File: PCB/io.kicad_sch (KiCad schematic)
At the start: 18 parts, among them J1 Conn_ARM_SWD_TagConnect_TC203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, J2 USB_C_Receptacle_USB2.0_16P, Q4 PMOS, U5 TLC59283RGER

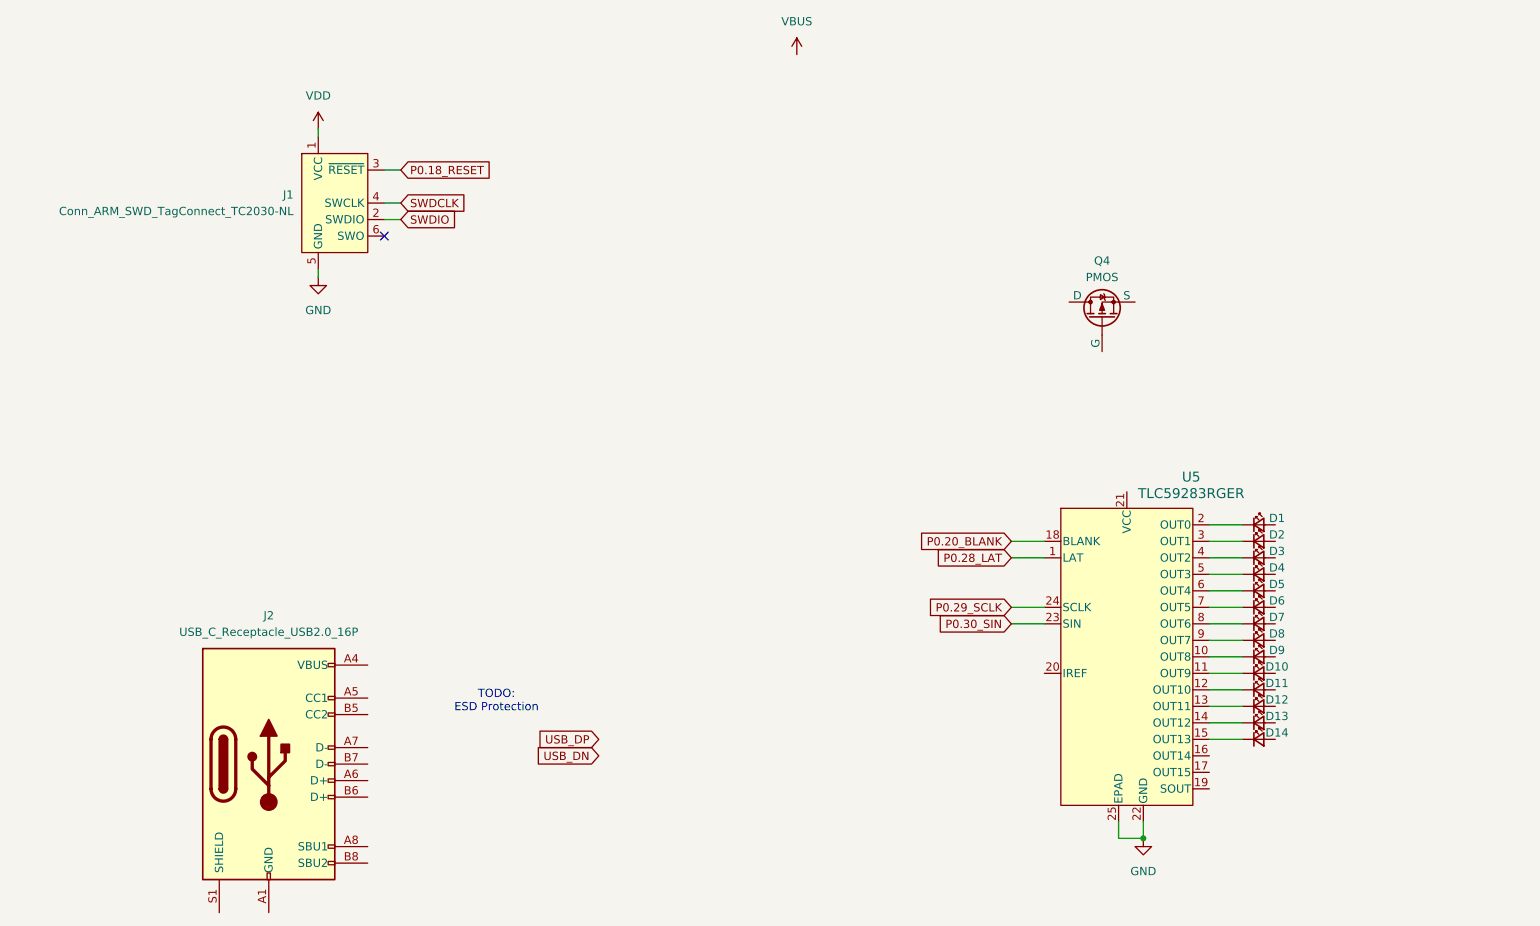
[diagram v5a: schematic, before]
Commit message: redid the pcb layout for a more bigger devboard approach. Added a few more components and the antenna.
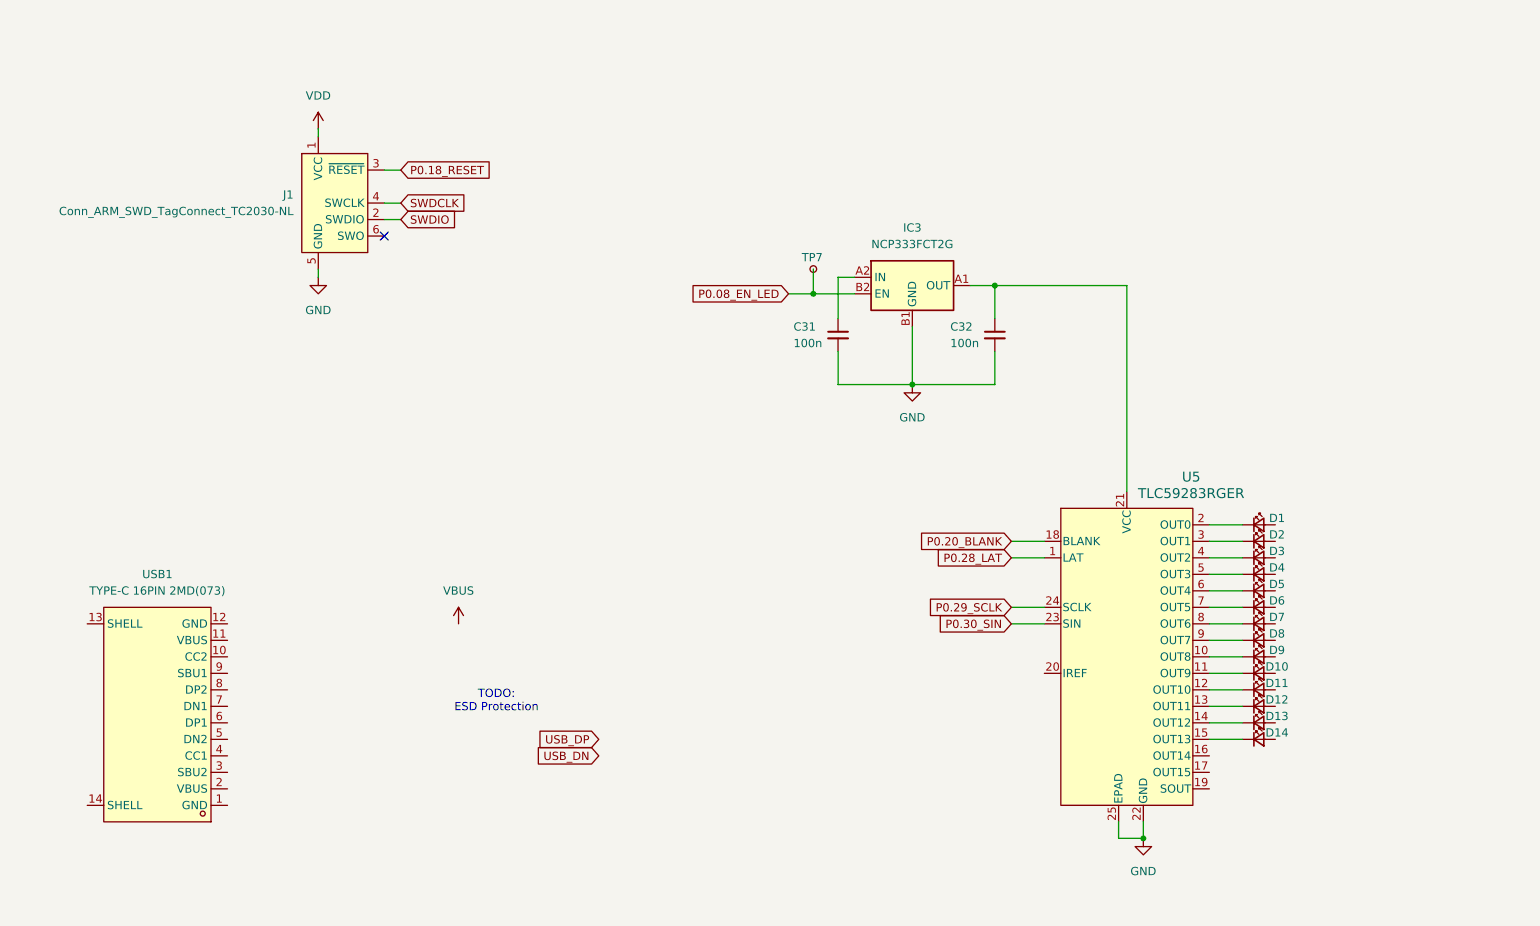
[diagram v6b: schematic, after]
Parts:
- removed J2: USB_C_Receptacle_USB2.0_16P, symbol Connector:USB_C_Receptacle_USB2.0_16P
- removed Q4: PMOS, symbol Simulation_SPICE:PMOS
- added C31, C32: 100n, Capacitor_SMD:C_0402_1005Metric, symbol Device:C_Small
- added IC3: NCP333FCT2G, BGA4C40P2X2_76X76X63, symbol NCP333FCT2G:NCP333FCT2G
- added TP7: TestPoint_Small, TestPoint:TestPoint_Pad_D1.0mm, symbol Connector:TestPoint_Small
- added USB1: TYPE-C 16PIN 2MD(073), USB-C-SMD_TYPE-C-6PIN-2MD-073:USB-C-SMD_TYPE-C-6PIN-2MD-073, symbol easyeda2kicad:TYPE-C16PIN2MD(073)
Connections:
- net GND: now also C31.2, C32.2, IC3.B1 (GND)
- net at U5.21 (VCC): now also C32.1, IC3.A1 (OUT)
- new net: C31.1, IC3.A2 (IN)
- new net P0.08_EN_LED: IC3.B2 (EN), TP7.1

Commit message: Added more Components
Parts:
- added C33: 100n, Capacitor_SMD:C_0402_1005Metric, symbol Device:C_Small
- added J2: LED, Connector_PinHeader_2.54mm:PinHeader_1x02_P2.54mm_Vertical, symbol Connector:Conn_01x02_Pin
- added R11, R12: 5k1, Resistor_SMD:R_0402_1005Metric, symbol Device:R_Small
- added R13: 5k3, Resistor_SMD:R_0402_1005Metric, symbol Device:R_Small
- added TP10, TP11, TP12, TP9: TestPoint_Small, TestPoint:TestPoint_Pad_D1.0mm, symbol Connector:TestPoint_Small
- added U7: SRV05-4, Package_TO_SOT_SMD:SOT-23-6, symbol Power_Protection:SRV05-4
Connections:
- net GND: now also USB1.1 (GND), USB1.12 (GND), USB1.13 (SHELL), USB1.14 (SHELL), C33.1, R11.2, R12.2, R13.1, U7.2 (VN)
- net P0.20_BLANK: now also TP12.1
- net P0.28_LAT: now also TP11.1
- net P0.29_SCLK: now also TP9.1
- net P0.30_SIN: now also TP10.1
- net USB_DN: now also U7.6 (IO4)
- net USB_DP: now also U7.4 (IO3)
- net VBUS: now also USB1.11 (VBUS), USB1.2 (VBUS), U7.5 (VP)
- net at C32.1, IC3.A1 (OUT): now also J2.2 (Pin_2); no longer U5.21 (VCC)
- net at USB1.10 (CC2): now also R11.1
- net at USB1.4 (CC1): now also R12.1
- net at USB1.5 (DN2): now also USB1.7 (DN1), U7.3 (IO2)
- net at USB1.6 (DP1): now also USB1.8 (DP2), U7.1 (IO1)
- net at U5.20 (IREF): now also R13.2
- net +3.3V: now reaches C31.1, IC3.A2 (IN)
- new net: C33.2, J2.1 (Pin_1), U5.21 (VCC)
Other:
- note removed: "TODO: ESD Protection"

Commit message: Continued on Devboard
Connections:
- net at C33.2, J2.1 (Pin_1), U5.21 (VCC): now also D1.2 (A), D10.2 (A), D11.2 (A), D12.2 (A), D13.2 (A), D14.2 (A), D2.2 (A), D3.2 (A), D4.2 (A), D5.2 (A), D6.2 (A), D7.2 (A), D8.2 (A), D9.2 (A)
- no-connect marks 1 -> 4
